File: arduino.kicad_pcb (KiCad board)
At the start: 2 copper layers, 92.2 x 73.7 mm, 29 parts, among them P1 CONN_25X2, P2 Arduino-Left, P3 Arduino-Bottom, P4 Arduino-FTDI, P5 Arduino_Right, P6 Arduino-Middle, U1 74LS32, U2 74LS08, U3 74LS540, U4 74LS74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

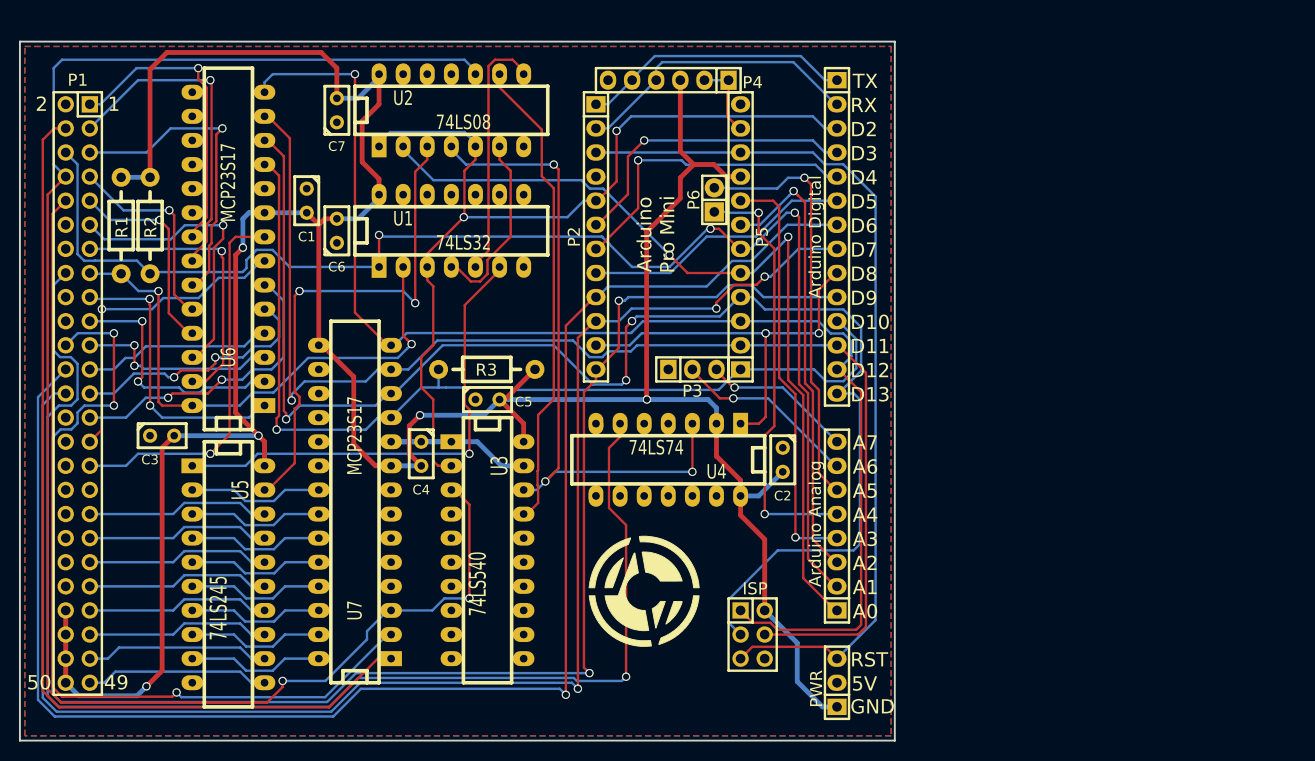
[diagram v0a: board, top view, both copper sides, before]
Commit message: Replace Arduino Pro Mini Clone with an ATMega32A instead
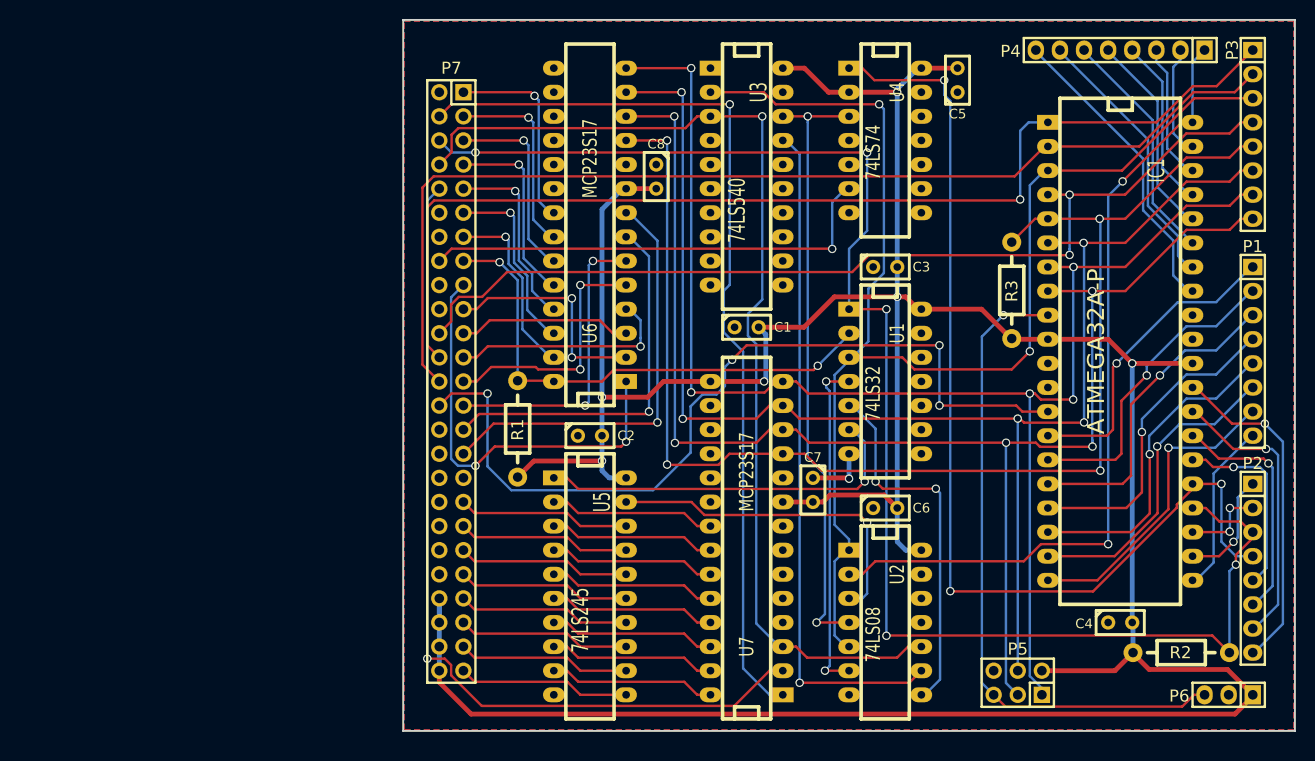
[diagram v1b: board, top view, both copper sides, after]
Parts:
- removed Arduino Analog: CONN_8, Socket_Strips:Socket_Strip_Straight_1x08
- removed Arduino Digital: CONN_14, Socket_Strips:Socket_Strip_Straight_1x14
- removed G***: LOGO, Own:logo
- removed G***: LOGO, Own:logo-back
- removed ISP: CONN_3X2, Pin_Headers:Pin_Header_Straight_2x03
- removed PWR: CONN_3, Socket_Strips:Socket_Strip_Straight_1x03
- added C8: C, Capacitors_ThroughHole:Capacitor3MMDiscRM2.5, F.Cu at (170.2, 88.9)
- added IC1: ATMEGA32A-P, Sockets_DIP:DIP-40__600_ELL, F.Cu at (219.1, 107.3)
- added P7: BUS, Socket_Strips:Socket_Strip_Straight_2x25, F.Cu at (148.6, 110.5)
- P1: value CONN_25X2 -> PORT_D; footprint Socket_Strips:Socket_Strip_Straight_2x25 -> Socket_Strips:Socket_Strip_Straight_1x08
- P2: value Arduino-Left -> PORT_C; footprint Socket_Strips:Socket_Strip_Straight_1x12 -> Socket_Strips:Socket_Strip_Straight_1x08
- P3: value Arduino-Bottom -> PORT_B; footprint Socket_Strips:Socket_Strip_Straight_1x03 -> Socket_Strips:Socket_Strip_Straight_1x08
- P4: value Arduino-FTDI -> PORT_A; footprint Socket_Strips:Socket_Strip_Straight_1x06 -> Socket_Strips:Socket_Strip_Straight_1x08
- P5: value Arduino_Right -> ISP; footprint Socket_Strips:Socket_Strip_Straight_1x12 -> Socket_Strips:Socket_Strip_Straight_2x03
- P6: value Arduino-Middle -> PWR; footprint Socket_Strips:Socket_Strip_Straight_1x02 -> Socket_Strips:Socket_Strip_Straight_1x03
- moved P1 123.9 mm to (233.0, 107.3)
- moved R2 117.6 mm to (225.4, 139.1), turned to 0 degrees
- moved C3 78.2 mm to (194.3, 98.4)
- moved P2 77.5 mm to (233.0, 130.2)
- moved C4 75.8 mm to (219.1, 135.9), turned to 0 degrees
- moved P6 75.2 mm to (230.5, 143.5), turned to 0 degrees
- moved U2 70.7 mm to (194.3, 135.9), turned to 270 degrees
- moved C6 64.7 mm to (194.3, 123.8), turned to 0 degrees
- moved C7 64.2 mm to (186.7, 121.9), turned to 270 degrees
- moved P3 64.0 mm to (233.0, 84.5), turned to 90 degrees
- moved C5 59.9 mm to (201.9, 78.7), turned to 90 degrees
- moved R3 55.9 mm to (207.6, 101.0), turned to 90 degrees
- moved P5 55.3 mm to (208.3, 142.2), turned to 0 degrees
- moved U1 48.4 mm to (194.3, 110.5), turned to 270 degrees
- moved C1 48.2 mm to (179.7, 104.8), turned to 0 degrees
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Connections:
- P1 pad 1: /A0 -> /TXD
- P1 pad 2: /M1 -> /RXI
- P1 pad 3: /A1 -> /DT10
- P1 pad 4: /MREQ -> /DT11
- P1 pad 5: /A2 -> /DT12
- P1 pad 6: /AN1 -> /DT13
- P1 pad 7: /A3 -> /DT14
- P1 pad 8: /WR -> /DT15
- P2 pad 1: /TXD -> /DT16
- P2 pad 2: /RXI -> /DT17
- P2 pad 3: /RST -> /DT18
- P2 pad 4: GND -> /CLRWT
- P2 pad 5: /AVRCS -> /DT20
- P2 pad 6: /DT3 -> /DT21
- P2 pad 7: /DT4 -> /DT22
- P2 pad 8: /DT5 -> /DT23
- P3 pad 1: GND -> /BUSRQ
- P3 pad 2: /AN6 -> /BUSAK
- P3 pad 3: /AN7 -> /AVRCS
- P4 pad 1: GND -> /AN0
- P4 pad 2: GND -> /AN1
- P4 pad 3: VCC -> /AN2
- P4 pad 4: /RXI -> /AN3
- P4 pad 5: /TXD -> /AN4
- P4 pad 6: /DTR -> /AN5
- P5 pad 1: /DT10 -> /DT6
- P5 pad 2: /DT11 -> VCC
- P5 pad 3: /DT12 -> /DT7
- P5 pad 4: /DT13 -> /DT5
- P5 pad 5: /AN0 -> /RST
- P5 pad 6: /AN1 -> GND
- P6 pad 1: /AN4 -> VCC
- P6 pad 2: /AN5 -> GND
- R2 pad 2: /AN1 -> /DT18
- R3 pad 2: /DT10 -> /DT4
- U1 pad 1: /AN1 -> /DT18
- U4 pad 1: /DT8 -> /CLRWT
- U6 pad 11: /DT10 -> /DT4
- U6 pad 12: /DT13 -> /DT7
- U6 pad 13: /DT11 -> /DT5
- U6 pad 14: /DT12 -> /DT6
- U7 pad 11: /DT10 -> /DT4
- U7 pad 12: /DT13 -> /DT7
- U7 pad 13: /DT11 -> /DT5
- U7 pad 14: /DT12 -> /DT6
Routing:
- net /DT9: track 172.3 -> 0.00 mm, vias 4 -> 0
- net /DT18: track 0.00 -> 159.3 mm, vias 0 -> 5
- net /DT6: track 0.00 -> 153.6 mm, vias 0 -> 5
- net /DT7: track 0.00 -> 153.1 mm, vias 0 -> 5
- net /AN1: track 140.6 -> 11.7 mm, vias 3 -> 0
- net /DT5: track 28.6 -> 154.2 mm, vias 0 -> 5
- net /DT13: track 150.8 -> 33.1 mm, vias 3 -> 1
- net /DT4: track 32.9 -> 141.5 mm, vias 1 -> 4
- net /CLRWT: track 0.00 -> 108.5 mm, vias 0 -> 3
- net /DT12: track 137.2 -> 33.8 mm
- net /DT11: track 135.1 -> 33.5 mm
- net /WAIT: track 139.8 -> 49.2 mm
- net /CLK: track 0.00 -> 90.4 mm, vias 0 -> 4
- net /DT3: track 31.9 -> 102.0 mm, vias 1 -> 2
- net /DT10: track 102.0 -> 33.3 mm
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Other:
- board size 92.2 x 73.7 mm -> 94 x 74.9 mm
- board text removed: "1"
- board text removed: "2"
- board text removed: "49"
- board text removed: "50"
- board text removed: "5V"
- board text removed: "A0"
- board text removed: "A1"
- board text removed: "A2"
- board text removed: "A3"
- board text removed: "A4"
- board text removed: "A5"
- board text removed: "A6"
- board text removed: "A7"
- board text removed: "Arduino Pro Mini"
- board text removed: "D10"
- board text removed: "D11"
- board text removed: "D12"
- board text removed: "D13"
- board text removed: "D2"
- board text removed: "D3"
- board text removed: "D4"
- board text removed: "D5"
- board text removed: "D6"
- board text removed: "D7"
- board text removed: "D8"
- board text removed: "D9"
- board text removed: "GND"
- board text removed: "RST"
- board text removed: "RX"
- board text removed: "TX"

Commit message: Some changes to fill zones better
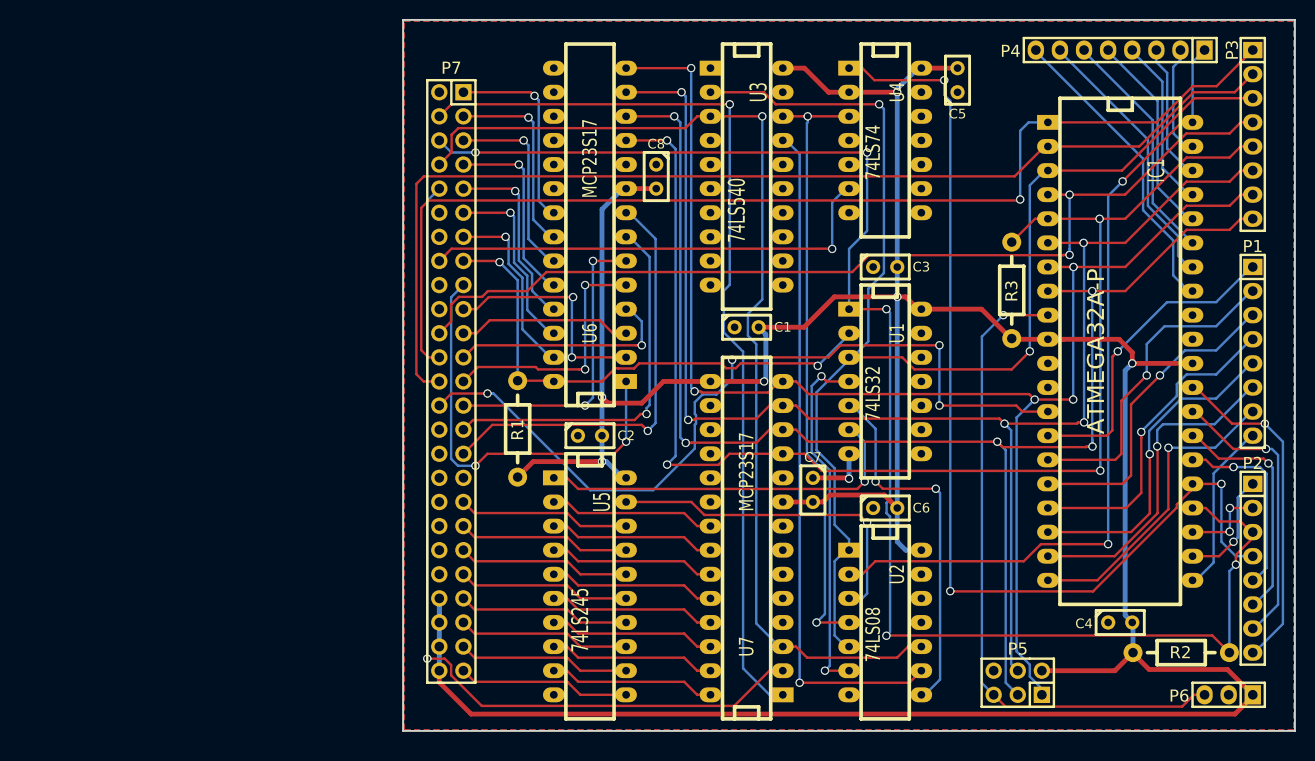
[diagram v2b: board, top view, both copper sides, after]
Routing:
- net /CLK: track 90.4 -> 86.0 mm
- net Net-(U1-Pad4): track 35.8 -> 38.1 mm
- net /BUSAK: track 113.6 -> 115.7 mm
- net /AVRCS: track 145.5 -> 147.1 mm
- net /BUSRQ: track 114.4 -> 116.0 mm
- net /RXI: track 32.8 -> 34.2 mm
- net VCC: track 359.2 -> 360.4 mm
- net /DT13: track 33.1 -> 34.1 mm
- net /DT4: track 141.5 -> 142.3 mm
- net /TXD: track 32.8 -> 33.5 mm
- net /A7: track 54.3 -> 54.9 mm
- net /DT18: track 159.3 -> 159.9 mm

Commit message: Silkscreen texts and a jumper to select system clock or feed a separate one for the AVR
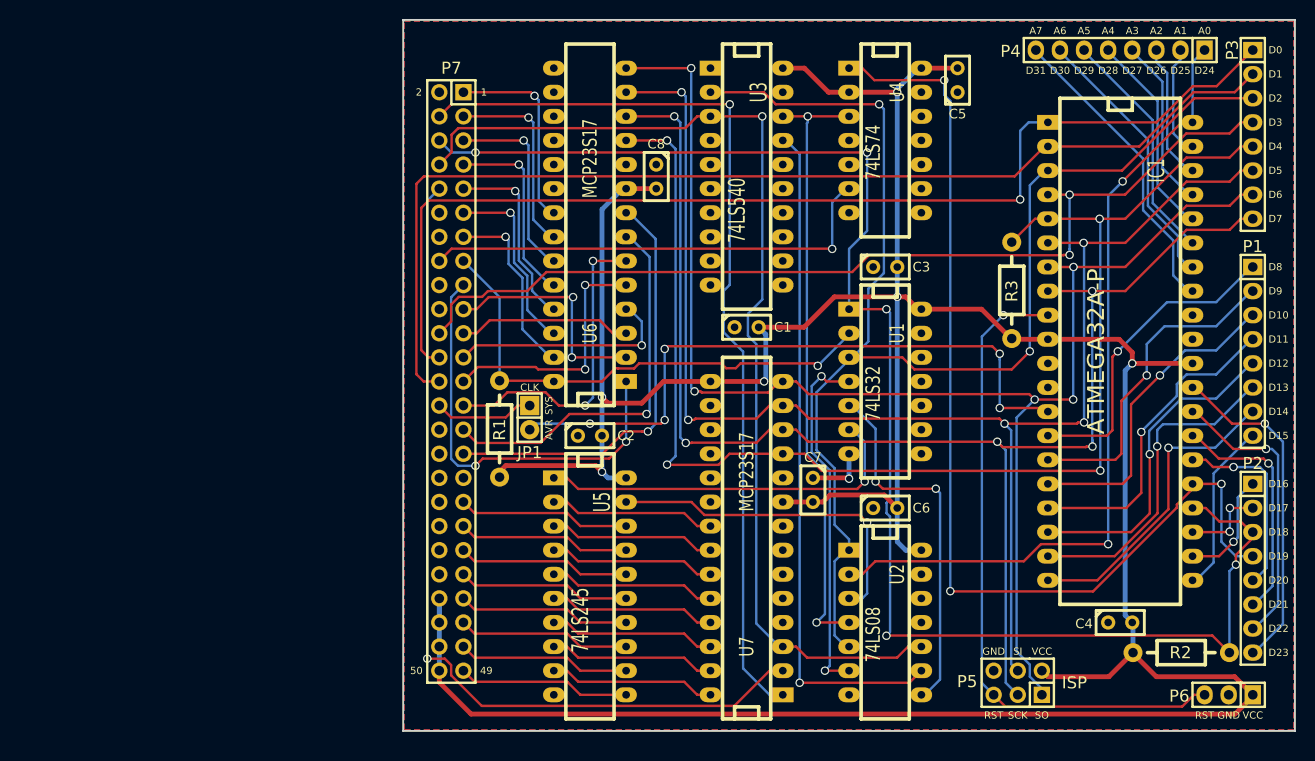
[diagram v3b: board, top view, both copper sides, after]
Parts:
- added JP1: JUMPER, Socket_Strips:Socket_Strip_Straight_1x02, F.Cu at (156.8, 114.3)
- moved R1 1.91 mm to (153.7, 115.6)
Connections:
- IC1 pad 13: /CLK -> /XTAL
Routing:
- net /CLK: track 86.0 -> 10.6 mm, vias 4 -> 0
- net /XTAL: track 0.00 -> 68.8 mm, vias 0 -> 5
- net VCC: track 360.4 -> 363.9 mm
- net /A14: track 40.0 -> 41.2 mm
- net /A13: track 31.9 -> 33.1 mm
- net /A7: track 54.9 -> 53.9 mm, vias 2 -> 1
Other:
- board text added: "1"
- board text added: "2"
- board text added: "49"
- board text added: "50"
- board text added: "A0"
- board text added: "A1"
- board text added: "A2"
- board text added: "A3"
- board text added: "A4"
- board text added: "A5"
- board text added: "A6"
- board text added: "A7"
- board text added: "AVR"
- board text added: "CLK"
- board text added: "D0"
- board text added: "D1"
- board text added: "D10"
- board text added: "D11"
- board text added: "D12"
- board text added: "D13"
- board text added: "D14"
- board text added: "D15"
- board text added: "D16"
- board text added: "D17"
- board text added: "D18"
- board text added: "D19"
- board text added: "D2"
- board text added: "D20"
- board text added: "D21"
- board text added: "D22"
- board text added: "D23"
- board text added: "D24"
- board text added: "D25"
- board text added: "D26"
- board text added: "D27"
- board text added: "D28"
- board text added: "D29"
- board text added: "D3"
- board text added: "D30"
- board text added: "D31"
- board text added: "D4"
- board text added: "D5"
- board text added: "D6"
- board text added: "D7"
- board text added: "D8"
- board text added: "D9"
- board text added: "GND"
- board text added: "ISP"
- board text added: "RST"
- board text added: "SCK"
- board text added: "SI"
- board text added: "SO"
- board text added: "SYS"
- board text added: "VCC"

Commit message: Some silkscreen updates
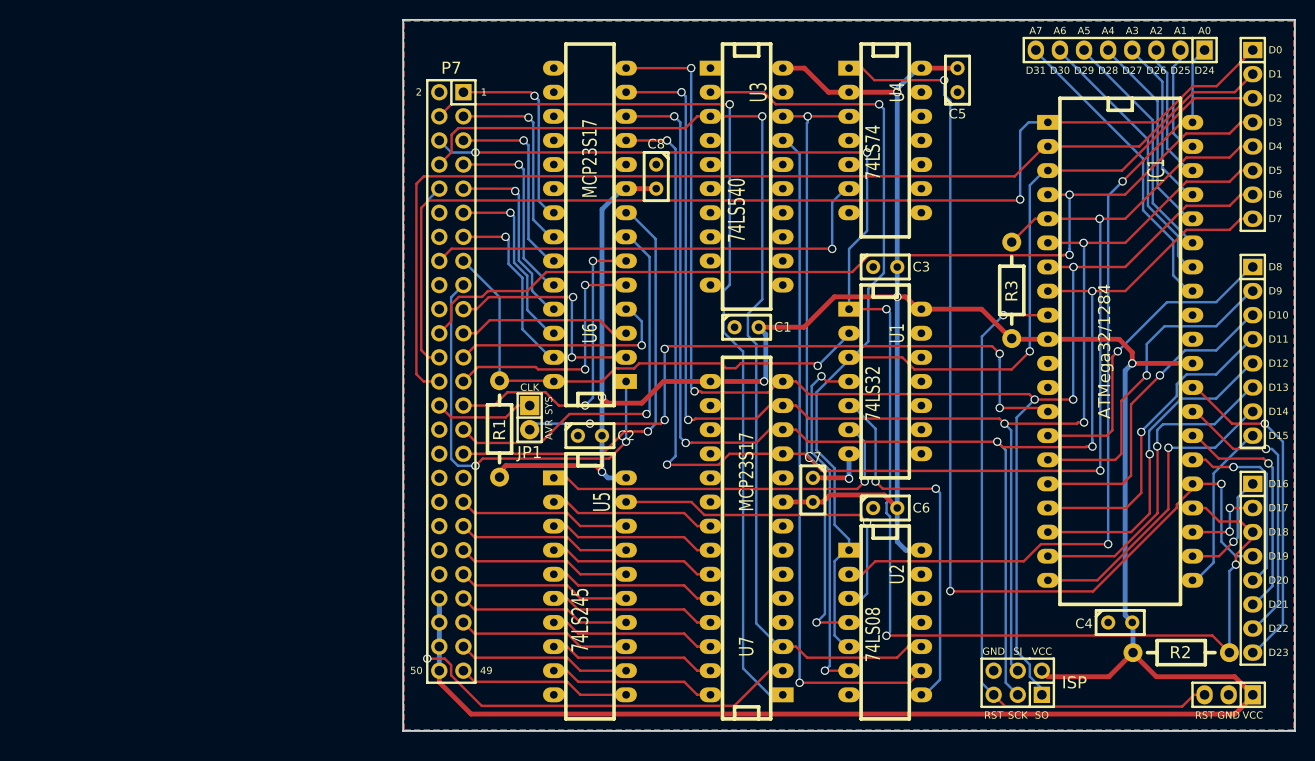
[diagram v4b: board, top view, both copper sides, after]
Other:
- board text added: "ATMega32/1284"

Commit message: Fix a bug and add an FTDI connector
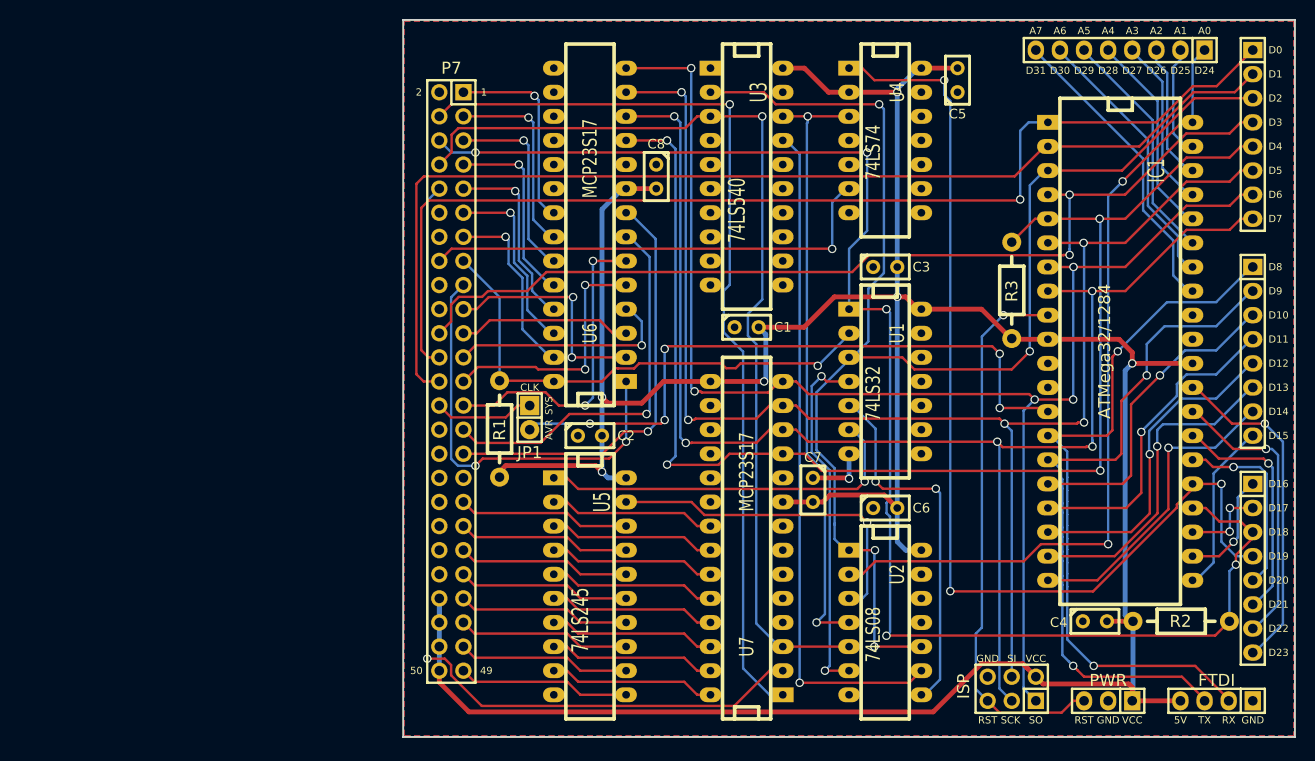
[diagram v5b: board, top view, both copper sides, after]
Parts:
- added P8: CONN_4, Socket_Strips:Socket_Strip_Straight_1x04, F.Cu at (229.2, 144.1)
- moved P6 12.7 mm to (217.8, 144.1)
- moved R2 3.30 mm to (225.4, 135.8)
- moved C4 2.67 mm to (216.4, 135.8)
- moved P5 0.90 mm to (207.6, 142.9)
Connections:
- U2 pad 10: /WR -> /AVRCS
- U2 pad 5: /AVRCS -> /WR
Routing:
- net /TXD: track 33.5 -> 75.8 mm, vias 1 -> 2
- net /RXI: track 34.2 -> 72.7 mm, vias 1 -> 2
- net VCC: track 363.9 -> 342.4 mm
- net /RST: track 69.4 -> 58.2 mm
- net /WR: track 111.0 -> 102.4 mm
- net /AVRCS: track 147.1 -> 153.4 mm, vias 2 -> 4
- net /DT18: track 159.9 -> 156.5 mm
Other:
- board size 94 x 74.9 mm -> 94 x 75.6 mm
- board text added: "5V"
- board text added: "FTDI"
- board text added: "PWR"
- board text added: "RX"
- board text added: "TX"
